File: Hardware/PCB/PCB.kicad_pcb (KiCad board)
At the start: 4 copper layers, 95 x 70.5 mm, 108 parts, among them IC3 MPX5500DP, IC4 MPX5500DP, J1 Pump Motor, J13 Solenoid Terminal, J14 Solenoid Terminal, J15 Solenoid Terminal, J16 Solenoid Terminal, J17 Solenoid Terminal, J18 Programmer, J2 Pump Motor, J3 BLDC Motor, J4 BLDC Motor, J6 XUNPU DC-005-A250, J7 Solenoid Terminal, Q1 MMBT2222A, Q2 MMBT2222A, Q3 MMBT2222A, Q4 MMBT2222A, Q5 MMBT2222A, Q6 MMBT2222A, U1 ER-TFTM032-3, U10 AZ1117-5.0, U11 ESP32-S3-WROOM-1U-N16R8, U12 AZ1117-3.3, U2 SN74LVC2T45DCUR, U3 DRV8871DDA, U4 SPX5205M5-L-5-0/TR, U6 ADS1232IPW, U8 DRV8871DDA, U9 LMR16030PDDAR

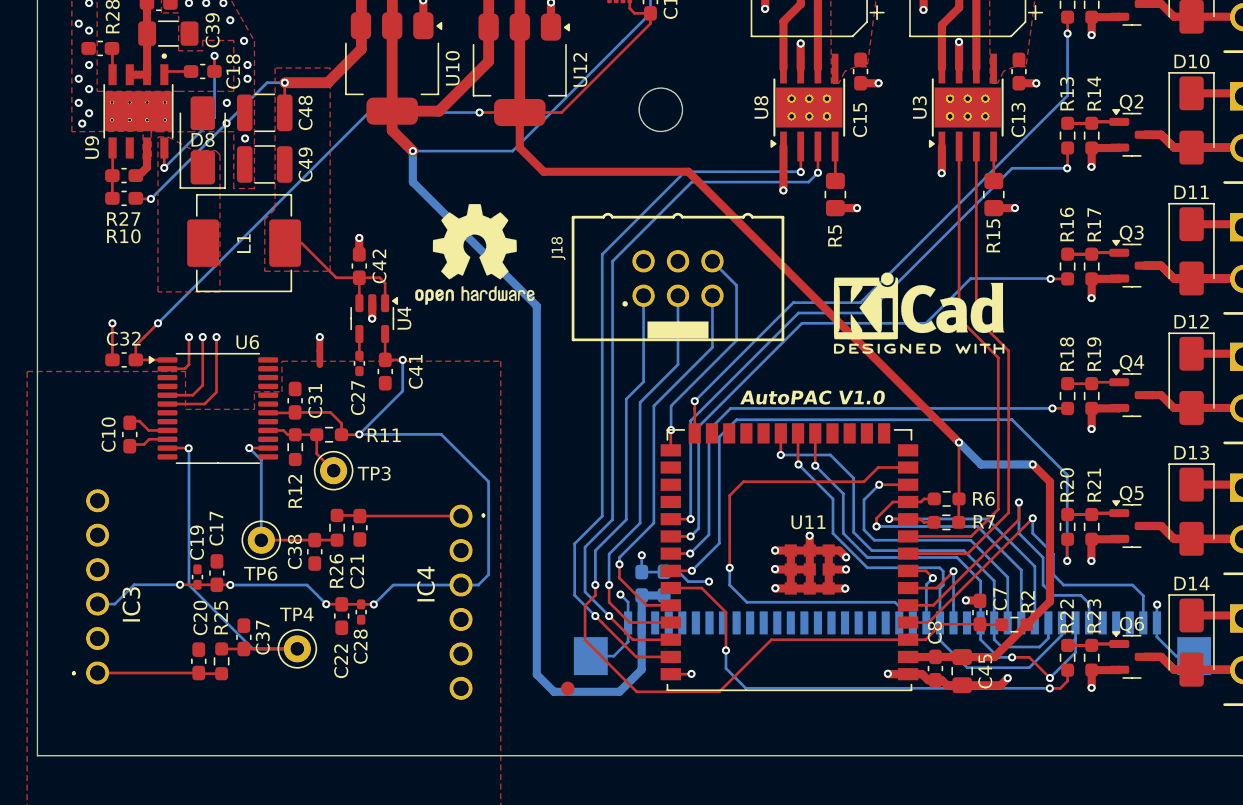
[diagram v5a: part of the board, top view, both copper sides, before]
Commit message: fixed various hole sizes, fixed unconnected signals to ADC, pcbs have been ordered
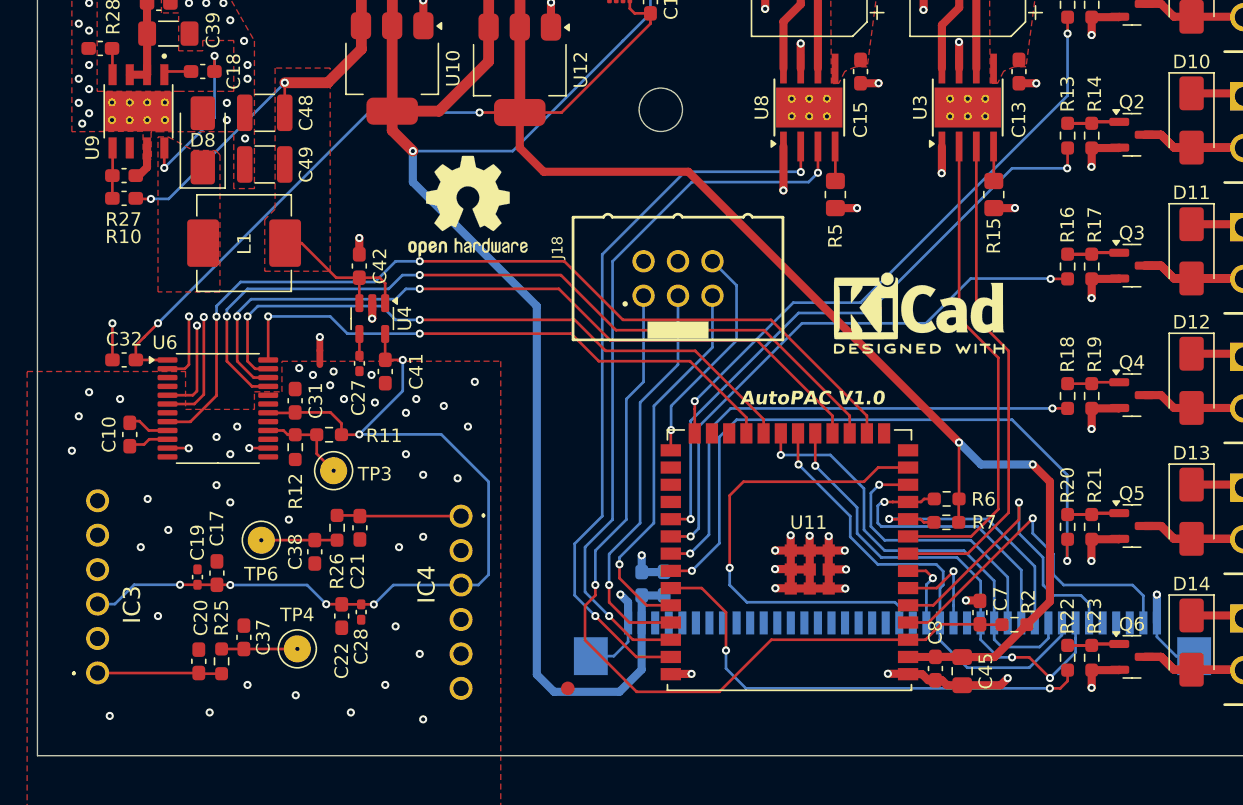
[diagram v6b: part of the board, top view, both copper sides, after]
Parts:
- moved REF** 3.59 mm to (207.3, 59.7)
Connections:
- J6 pad 3: GND -> (no net)
- U6 pad 21: /sensors/SPEED -> /GPIO9
- U6 pad 22: /sensors/PWDN -> /GPIO10
- U6 pad 23: /sensors/SCLK -> /GPIO14
- U6 pad 24: /sensors/DOUT -> /GPIO21
- U6 pad 8: /sensors/INPUT_MUX -> /GPIO46
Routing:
- net /GPIO46: track 0.00 -> 66.4 mm, vias 0 -> 2
- net /GPIO9: track 0.00 -> 60.2 mm, vias 0 -> 2
- net /GPIO10: track 0.00 -> 56.2 mm, vias 0 -> 2
- net /GPIO14: track 0.00 -> 47.9 mm, vias 0 -> 2
- net /GPIO21: track 0.00 -> 42.7 mm, vias 0 -> 2
- net GND: track 142.6 -> 144.4 mm, vias 64 -> 66
- net /SPI-MOSI: track 36.1 -> 34.7 mm
- net /DISP-BACKLIGHT: track 21.3 -> 20.5 mm
- net /SPI-CLK: track 34.7 -> 34.1 mm
- net /SPI-MISO: track 33.5 -> 32.9 mm
- net GNDA: vias 0 -> 40
- net +5.5V: vias 3 -> 2
- added copper zone on In2.Cu, net GNDA
